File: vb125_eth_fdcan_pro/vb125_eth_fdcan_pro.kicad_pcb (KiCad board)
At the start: 2 copper layers, 2 parts, among them U1 STM32H725IGKx, U2 LAN8740A

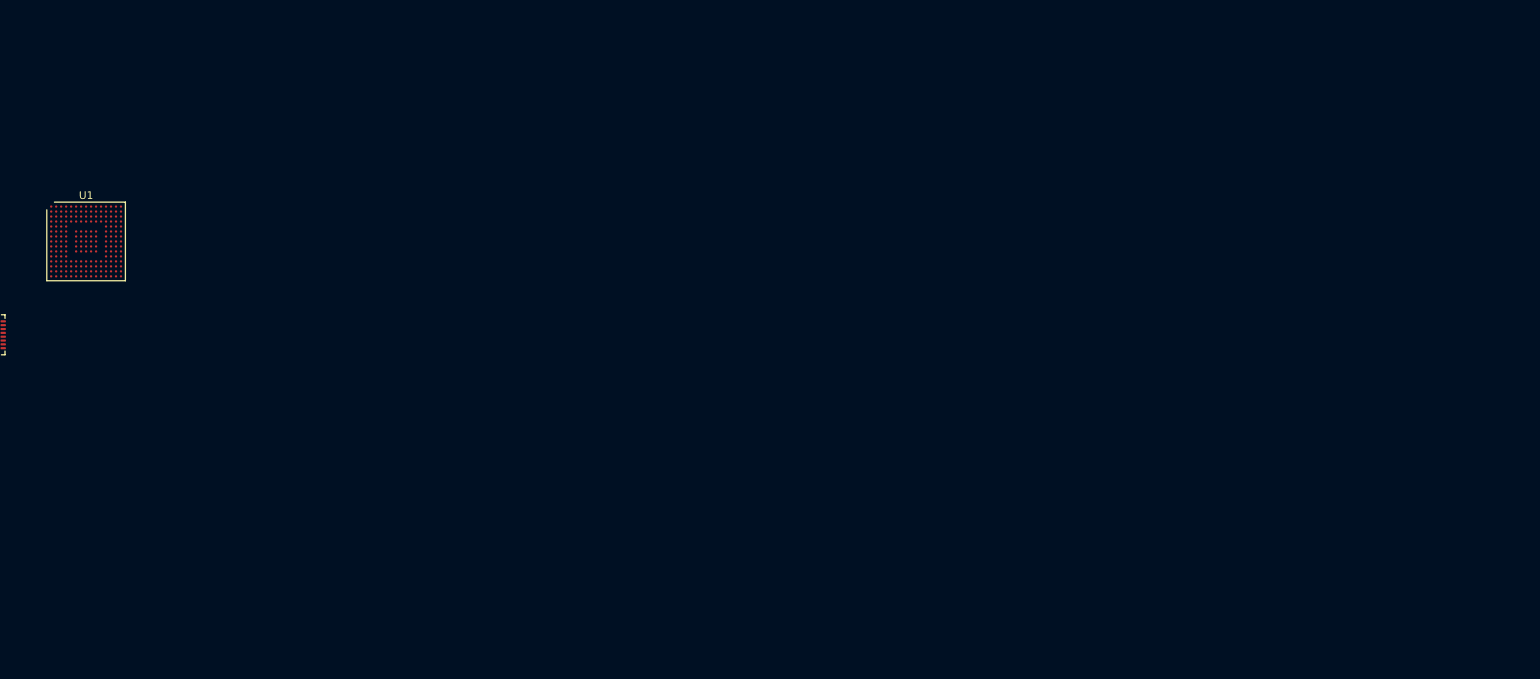
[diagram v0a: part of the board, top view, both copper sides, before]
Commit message: Work on PoE. Rearrange pages.
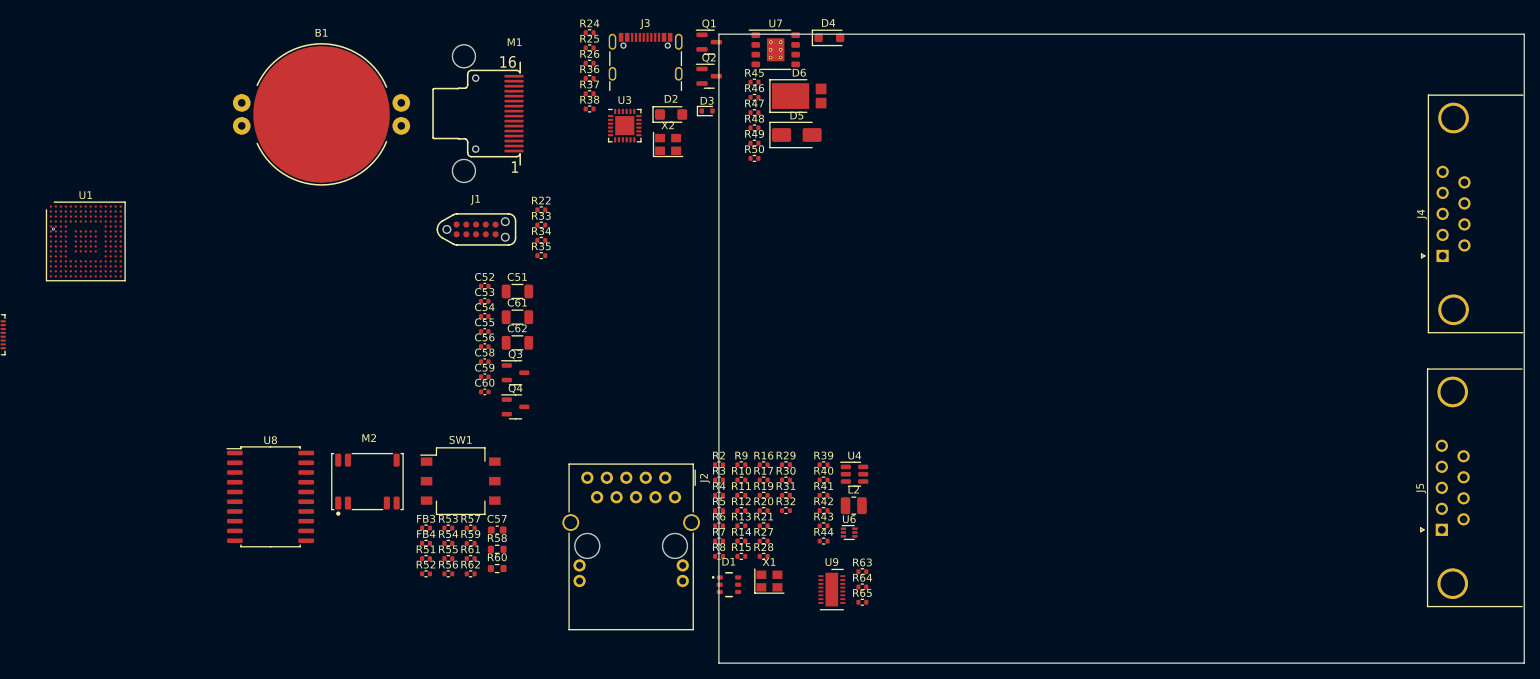
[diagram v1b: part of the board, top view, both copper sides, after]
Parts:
- added B1: BAT-HLD-001-THM, vhrd_connector_battery:BAT-HLD-001-THM, F.Cu at (97.4, 48.3)
- added C51: 10.0uF ±10% 10V X7R, Capacitor_SMD:C_1206_3216Metric, F.Cu at (122.9, 71.3)
- added C52: 50V_100nF_X7R, Capacitor_SMD:C_0402_1005Metric, F.Cu at (118.7, 70.7)
- added C53: X7R_10nF_50V, Capacitor_SMD:C_0402_1005Metric, F.Cu at (118.7, 72.6)
- added C54: 50V_100nF_X7R, Capacitor_SMD:C_0402_1005Metric, F.Cu at (118.7, 74.6)
- added C55: X7R_10nF_50V, Capacitor_SMD:C_0402_1005Metric, F.Cu at (118.7, 76.6)
- added C56: 5.0pF, Capacitor_SMD:C_0402_1005Metric, F.Cu at (118.7, 78.5)
- added C57: 4.7uF ±10% 6.3V, Capacitor_SMD:C_0603_1608Metric, F.Cu at (120.3, 102.5)
- added C58: 10.0nF ±10% 50V X7R, Capacitor_SMD:C_0402_1005Metric, F.Cu at (118.7, 80.5)
- added C59: 0.1uF 10% X7R 50V, Capacitor_SMD:C_0402_1005Metric, F.Cu at (118.7, 82.5)
- added C60: 220.0nF ±10% 10V X7R, Capacitor_SMD:C_0402_1005Metric, F.Cu at (118.7, 84.4)
- added C61: 10.0uF ±10% 10V X7R, Capacitor_SMD:C_1206_3216Metric, F.Cu at (122.9, 74.7)
- added C62: 10.0uF ±10% 10V X7R, Capacitor_SMD:C_1206_3216Metric, F.Cu at (122.9, 78.0)
- added D1: D5V0P4UR6SO-7, vhrd_passive_tvs:D5V0P4UR6SO-7, F.Cu at (150.5, 109.6)
- added D2: SMF22A, Diode_SMD:D_SMF, F.Cu at (143.0, 48.3)
- added D3: MM5Z10VT1G, Diode_SMD:D_SOD-523, F.Cu at (147.7, 47.8)
- added D4: RB168MM150TFTR, Diode_SMD:D_SOD-123F, F.Cu at (163.6, 38.3)
- added D5: CMZ5944B, Diode_SMD:D_SMA, F.Cu at (159.4, 50.9)
- added D6: PDS835L-13, Diode_SMD:D_PowerDI-5, F.Cu at (159.7, 45.9)
- added FB3: 100MHz_1.8KOhm, Resistor_SMD:R_0402_1005Metric, F.Cu at (111.0, 102.2)
- added FB4: BLM15BX182SN1D_100MHz_1.8KOhm, Resistor_SMD:R_0402_1005Metric, F.Cu at (111.0, 104.2)
- added J1: TAGconnect NL, vhrd_connector_debug:TC2050-IDC-NL, F.Cu at (117.5, 63.3)
- added J2: ARJM11C7-114-BA-EW2, vhrd_connector_abracon:RJ45_Abracon_ARJM11_7POE_LED, F.Cu at (132.0, 95.6)
- added J3: USB_C_Receptacle_USB2.0, Connector_USB:USB_C_Receptacle_GCT_USB4105-xx-A_16P_TopMnt_Horizontal, F.Cu at (139.6, 41.9)
- added J4: D09P33E4GL00LF, vhrd_connector_amphenol:D09P33E4GL00LF, F.Cu at (243.6, 66.7)
- added J5: D09P33E4GL00LF, vhrd_connector_amphenol:D09P33E4GL00LF, F.Cu at (243.4, 102.4)
- added L2: DFE252010F-1R0M=P2, Inductor_SMD:L_1008_2520Metric, F.Cu at (166.8, 99.3)
- added M1: DM-OLED042-647, vhrd_opto_display:DM-OLED042-647, F.Cu at (122.5, 48.2)
- added M2: B0505MT-1WR4, vhrd_module_power:B0505MT-1WR4, F.Cu at (103.4, 96.1)
- added Q1: BSS138, Package_TO_SOT_SMD:SOT-23, F.Cu at (147.9, 38.8)
- added Q2: BSS138, Package_TO_SOT_SMD:SOT-23, F.Cu at (147.9, 43.3)
- added Q3: FDN358P, Package_TO_SOT_SMD:SOT-23-3, F.Cu at (122.7, 81.9)
- added Q4: FDN358P, Package_TO_SOT_SMD:SOT-23-3, F.Cu at (122.7, 86.4)
- added R10: 10k, Resistor_SMD:R_0402_1005Metric, F.Cu at (152.1, 95.9)
- added R11: 33R, Resistor_SMD:R_0402_1005Metric, F.Cu at (152.1, 97.9)
- added R12: 33R, Resistor_SMD:R_0402_1005Metric, F.Cu at (152.1, 99.9)
- added R13: 33R, Resistor_SMD:R_0402_1005Metric, F.Cu at (152.1, 101.9)
- added R14: 10k, Resistor_SMD:R_0402_1005Metric, F.Cu at (152.1, 103.9)
- added R15: 10k, Resistor_SMD:R_0402_1005Metric, F.Cu at (152.1, 105.9)
- added R16: 10k, Resistor_SMD:R_0402_1005Metric, F.Cu at (155.0, 93.9)
- added R17: 12k1, Resistor_SMD:R_0402_1005Metric, F.Cu at (155.0, 95.9)
- added R19: ?R, Resistor_SMD:R_0402_1005Metric, F.Cu at (155.0, 97.9)
- added R2: 10k, Resistor_SMD:R_0402_1005Metric, F.Cu at (149.2, 93.9)
- added R20: ?R, Resistor_SMD:R_0402_1005Metric, F.Cu at (155.0, 99.9)
- added R21: ?R, Resistor_SMD:R_0402_1005Metric, F.Cu at (155.0, 101.9)
- added R22: 49R9, Resistor_SMD:R_0402_1005Metric, F.Cu at (126.0, 60.7)
- added R24: ?R, Resistor_SMD:R_0402_1005Metric, F.Cu at (132.3, 37.6)
- added R25: ?R, Resistor_SMD:R_0402_1005Metric, F.Cu at (132.3, 39.6)
- added R26: ?R, Resistor_SMD:R_0402_1005Metric, F.Cu at (132.3, 41.6)
- added R27: 49R9, Resistor_SMD:R_0402_1005Metric, F.Cu at (155.0, 103.9)
- added R28: 49R9, Resistor_SMD:R_0402_1005Metric, F.Cu at (155.0, 105.9)
- added R29: 49R9, Resistor_SMD:R_0402_1005Metric, F.Cu at (157.9, 93.9)
- added R3: 10k, Resistor_SMD:R_0402_1005Metric, F.Cu at (149.2, 95.9)
- added R30: 49R9, Resistor_SMD:R_0402_1005Metric, F.Cu at (157.9, 95.9)
- added R31: 1K, Resistor_SMD:R_0402_1005Metric, F.Cu at (157.9, 97.9)
- added R32: 1K, Resistor_SMD:R_0402_1005Metric, F.Cu at (157.9, 99.9)
- added R33: 0, Resistor_SMD:R_0402_1005Metric, F.Cu at (126.0, 62.7)
- added R34: 10K, Resistor_SMD:R_0402_1005Metric, F.Cu at (126.0, 64.7)
- added R35: 10K, Resistor_SMD:R_0402_1005Metric, F.Cu at (126.0, 66.7)
- added R36: 5K1, Resistor_SMD:R_0402_1005Metric, F.Cu at (132.3, 43.6)
- added R37: 5K1, Resistor_SMD:R_0402_1005Metric, F.Cu at (132.3, 45.6)
- added R38: 5K1, Resistor_SMD:R_0402_1005Metric, F.Cu at (132.3, 47.6)
- added R39: 301K, Resistor_SMD:R_0402_1005Metric, F.Cu at (162.8, 93.9)
- added R4: 10k, Resistor_SMD:R_0402_1005Metric, F.Cu at (149.2, 97.9)
- added R40: 0, Resistor_SMD:R_0402_1005Metric, F.Cu at (162.8, 95.9)
- added R41: 100K, Resistor_SMD:R_0402_1005Metric, F.Cu at (162.8, 97.9)
- added R42: 100K, Resistor_SMD:R_0402_1005Metric, F.Cu at (162.8, 99.9)
- added R43: 45k, Resistor_SMD:R_0402_1005Metric, F.Cu at (162.8, 101.9)
- added R44: 10k, Resistor_SMD:R_0402_1005Metric, F.Cu at (162.8, 103.9)
- added R45: 1M, Resistor_SMD:R_0402_1005Metric, F.Cu at (153.8, 44.1)
- added R46: 348K, Resistor_SMD:R_0402_1005Metric, F.Cu at (153.8, 46.0)
- added R47: 10K, Resistor_SMD:R_0402_1005Metric, F.Cu at (153.8, 48.0)
- added R48: ?R, Resistor_SMD:R_0402_1005Metric, F.Cu at (153.8, 50.0)
- added R49: 158K, Resistor_SMD:R_0402_1005Metric, F.Cu at (153.8, 52.0)
- added R5: 10k, Resistor_SMD:R_0402_1005Metric, F.Cu at (149.2, 99.9)
- added R50: 100R, Resistor_SMD:R_0402_1005Metric, F.Cu at (153.8, 54.0)
- added R51: 0, Resistor_SMD:R_0402_1005Metric, F.Cu at (111.0, 106.2)
- added R52: 47K 1%, Resistor_SMD:R_0402_1005Metric, F.Cu at (111.0, 108.2)
- added R53: 0, Resistor_SMD:R_0402_1005Metric, F.Cu at (113.9, 102.2)
- added R54: 47K 1%, Resistor_SMD:R_0402_1005Metric, F.Cu at (113.9, 104.2)
- added R55: 0, Resistor_SMD:R_0402_1005Metric, F.Cu at (113.9, 106.2)
- added R56: 100K 1%, Resistor_SMD:R_0402_1005Metric, F.Cu at (113.9, 108.2)
- added R57: 0, Resistor_SMD:R_0402_1005Metric, F.Cu at (116.8, 102.2)
- added R58: 56R, Resistor_SMD:R_0603_1608Metric, F.Cu at (120.3, 105.0)
- added R59: 100K 1%, Resistor_SMD:R_0402_1005Metric, F.Cu at (116.8, 104.2)
- added R6: 10k, Resistor_SMD:R_0402_1005Metric, F.Cu at (149.2, 101.9)
- added R60: 56R, Resistor_SMD:R_0603_1608Metric, F.Cu at (120.3, 107.5)
- added R61: 0, Resistor_SMD:R_0402_1005Metric, F.Cu at (116.8, 106.2)
- added R62: 0, Resistor_SMD:R_0402_1005Metric, F.Cu at (116.8, 108.2)
- added R63: DNP, Resistor_SMD:R_0402_1005Metric, F.Cu at (167.9, 107.9)
- added R64: DNP, Resistor_SMD:R_0402_1005Metric, F.Cu at (167.9, 109.9)
- added R65: DNP, Resistor_SMD:R_0402_1005Metric, F.Cu at (167.9, 111.9)
- added R7: 1k5, Resistor_SMD:R_0402_1005Metric, F.Cu at (149.2, 103.9)
- added R8: 10k, Resistor_SMD:R_0402_1005Metric, F.Cu at (149.2, 105.9)
- added R9: 10k, Resistor_SMD:R_0402_1005Metric, F.Cu at (152.1, 93.9)
- added SW1: DS04-254-2-03BK-SMT, Button_Switch_SMD:SW_DIP_SPSTx03_Slide_Omron_A6S-310x_W8.9mm_P2.54mm, F.Cu at (115.5, 96.1)
- added U3: USB3315, vhrd_interface_usb:QFN24_MICROCHIP, F.Cu at (136.9, 49.7)
- added U4: AOZ1282CI, Package_TO_SOT_SMD:SOT-23-6, F.Cu at (166.9, 95.2)
- added U6: RT5760A/B, Package_TO_SOT_SMD:SOT-563, F.Cu at (166.2, 102.8)
- added U7: LT8304IS8E#PBF, vhrd_generic:SOIC-8-ANALOG, F.Cu at (156.6, 39.8)
- added U8: ADM3057E, Package_SO:SOIC-20W_7.5x12.8mm_P1.27mm, F.Cu at (90.7, 98.1)
- added U9: LTC4267, Package_DFN_QFN:DFN-16-1EP_3x5mm_P0.5mm_EP1.66x4.4mm, F.Cu at (163.9, 110.2)
- added X1: 50MHz, Oscillator:Oscillator_SMD_Abracon_ASE-4Pin_3.2x2.5mm, F.Cu at (155.8, 109.1)
- added X2: 24MHz, Oscillator:Oscillator_SMD_Abracon_ASE-4Pin_3.2x2.5mm, F.Cu at (142.6, 52.2)
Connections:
- U1 pad A10: unconnected-(U1D-PD1-PadA10) -> FDCAN1_TX
- U1 pad A12: unconnected-(U1A-PA14-PadA12) -> /MCU_H7/H7_SWCLK
- U1 pad A13: unconnected-(U1I-VDDLDO-PadA13) -> /MCU_H7/VDDLDO
- U1 pad A14: unconnected-(U1I-VCAP-PadA14) -> /MCU_H7/VCAP
- U1 pad A2: unconnected-(U1B-PB8-PadA2) -> FDCAN1_RX
- U1 pad A3: unconnected-(U1I-VDDLDO-PadA3) -> /MCU_H7/VDDLDO
- U1 pad A4: unconnected-(U1I-VCAP-PadA4) -> /MCU_H7/VCAP
- U1 pad A7: unconnected-(U1G-PG11-PadA7) -> ETH_TXEN
- U1 pad A8: unconnected-(U1G-PG9-PadA8) -> FDCAN3_TX
- U1 pad B10: unconnected-(U1D-PD2-PadB10) -> SDMMC_CMD
- U1 pad B11: unconnected-(U1C-PC12-PadB11) -> SDMMC_CK
- U1 pad B13: unconnected-(U1A-PA13-PadB13) -> /MCU_H7/H7_SWDIO
- U1 pad B7: unconnected-(U1G-PG13-PadB7) -> ETH_TXD0
- U1 pad C11: unconnected-(U1C-PC11-PadC11) -> SDMMC_D3
- U1 pad C12: unconnected-(U1C-PC10-PadC12) -> SDMMC_D2
- U1 pad C5: unconnected-(U1I-BOOT0-PadC5) -> /MCU_H7/BOOT0
- U1 pad C6: unconnected-(U1B-PB5-PadC6) -> ULPI_D7
- U1 pad C7: unconnected-(U1G-PG14-PadC7) -> ETH_TXD1
- U1 pad C8: unconnected-(U1G-PG10-PadC8) -> FDCAN3_RX
- U1 pad D11: unconnected-(U1I-VDD-PadD11) -> +3V3_DCDC
- U1 pad D14: unconnected-(U1C-PC8-PadD14) -> SDMMC_D0
- U1 pad D4: unconnected-(U1I-PDR_ON-PadD4) -> Net-(U1I-PDR_ON)
- U1 pad D5: unconnected-(U1I-VDD-PadD5) -> +3V3_DCDC
- U1 pad E12: unconnected-(U1I-VDD-PadE12) -> +3V3_DCDC
- U1 pad E13: unconnected-(U1C-PC9-PadE13) -> SDMMC_D1
- U1 pad E15: unconnected-(U1I-VDD50USB-PadE15) -> +3V3_DCDC
- U1 pad E2: unconnected-(U1I-VBAT-PadE2) -> /MCU_H7/VBAT
- U1 pad E4: unconnected-(U1I-VDD-PadE4) -> +3V3_DCDC
- U1 pad F1: unconnected-(U1I-VLXSMPS-PadF1) -> /MCU_H7/VLX
- U1 pad F13: unconnected-(U1I-VDD33USB-PadF13) -> +3V3_DCDC
- U1 pad F2: unconnected-(U1I-VSSSMPS-PadF2) -> GND
- U1 pad G1: unconnected-(U1I-VDDSMPS-PadG1) -> /MCU_H7/VDDSMPS
- U1 pad G2: unconnected-(U1I-VFBSMPS-PadG2) -> /MCU_H7/VDDLDO
- U1 pad G4: unconnected-(U1I-VDD-PadG4) -> +3V3_DCDC
- U1 pad H12: unconnected-(U1I-VDD-PadH12) -> +3V3_DCDC
- U1 pad J1: unconnected-(U1H-PH0-OSC_IN-PadJ1) -> H7_CLK
- U1 pad K4: unconnected-(U1I-VDD-PadK4) -> +3V3_DCDC
- U1 pad L1: unconnected-(U1I-NRST-PadL1) -> /MCU_H7/~{H7_RST}
- U1 pad L12: unconnected-(U1I-VDD-PadL12) -> +3V3_DCDC
- U1 pad L15: unconnected-(U1B-PB13-PadL15) -> ULPI_D6
- U1 pad L2: unconnected-(U1C-PC0-PadL2) -> ULPI_STP
- U1 pad L3: unconnected-(U1C-PC1-PadL3) -> ETH_MDC
- U1 pad L4: unconnected-(U1I-VREF--PadL4) -> GND
- U1 pad M1: unconnected-(U1C-PC2-PadM1) -> ULPI_DIR
- U1 pad M15: unconnected-(U1B-PB12-PadM15) -> ULPI_D5
- U1 pad M2: unconnected-(U1C-PC3-PadM2) -> ULPI_NXT
- U1 pad M3: unconnected-(U1I-VREF+-PadM3) -> /MCU_H7/VDDA
- U1 pad M4: unconnected-(U1I-VDDA-PadM4) -> /MCU_H7/VDDA
- U1 pad M5: unconnected-(U1I-VDD-PadM5) -> +3V3_DCDC
- U1 pad M7: unconnected-(U1C-PC5-PadM7) -> ETH_RXD1
- U1 pad M8: unconnected-(U1B-PB1-PadM8) -> ULPI_D2
- U1 pad M9: unconnected-(U1I-VDD-PadM9) -> +3V3_DCDC
- U1 pad N12: unconnected-(U1B-PB10-PadN12) -> ULPI_D3
- U1 pad N3: unconnected-(U1I-VSSA-PadN3) -> GND
- U1 pad N4: /MCU_H7/TXD0 -> unconnected-(U1H-PH2-PadN4)
- U1 pad N5: unconnected-(U1A-PA3-PadN5) -> ULPI_D0
- U1 pad N6: unconnected-(U1A-PA7-PadN6) -> ETH_CRS_DV
- U1 pad P10: unconnected-(U1B-PB11-PadP10) -> ULPI_D4
- U1 pad P2: unconnected-(U1A-PA1-PadP2) -> ETH_REFCLK
- U1 pad P4: /MCU_H7/TXD2 -> unconnected-(U1H-PH4-PadP4)
- U1 pad P6: unconnected-(U1A-PA5-PadP6) -> ULPI_CK
- U1 pad R13: unconnected-(U1I-VCAP-PadR13) -> /MCU_H7/VCAP
- U1 pad R14: unconnected-(U1I-VDDLDO-PadR14) -> /MCU_H7/VDDLDO
- U1 pad R2: unconnected-(U1A-PA2-PadR2) -> ETH_MDIO
- U1 pad R4: /MCU_H7/TXD1 -> unconnected-(U1H-PH3-PadR4)
- U1 pad R5: /MCU_H7/TXD3 -> unconnected-(U1H-PH5-PadR5)
- U1 pad R6: unconnected-(U1C-PC4-PadR6) -> ETH_RXD0
- U1 pad R8: unconnected-(U1B-PB0-PadR8) -> ULPI_D1
- U2 pad 1: unconnected-(U2B-VDD2A-Pad1) -> /Eth/+AVDD_PHY
- U2 pad 10: unconnected-(U2A-RXD1/MODE1-Pad10) -> /Eth/RXD1
- U2 pad 11: unconnected-(U2A-RXD0/MODE0-Pad11) -> /Eth/RXD0
- U2 pad 12: unconnected-(U2B-VDDIO-Pad12) -> +3V3_DCDC
- U2 pad 13: unconnected-(U2A-RXER/RXD4/PHYAD0-Pad13) -> /Eth/PHYAD0
- U2 pad 15: unconnected-(U2A-COL/CRS_DV/MODE2-Pad15) -> Net-(U2A-COL/CRS_DV/MODE2)
- U2 pad 16: unconnected-(U2A-MDIO-Pad16) -> ETH_MDIO
- U2 pad 17: unconnected-(U2A-MDC-Pad17) -> ETH_MDC
- U2 pad 18: unconnected-(U2A-~{INT}/TXER/TXD4-Pad18) -> Net-(U2A-~{INT}/TXER/TXD4)
- U2 pad 19: unconnected-(U2A-~{RST}-Pad19) -> ~{ETH_PHY_RST}
- U2 pad 2: unconnected-(U2A-LED2/~{INT}/~{PME}/~{INTSEL}-Pad2) -> ~{ETH_INT_PME}
- U2 pad 21: unconnected-(U2A-TXEN-Pad21) -> ETH_TXEN
- U2 pad 22: /Eth/TXD0 -> ETH_TXD0
- U2 pad 23: /Eth/TXD1 -> ETH_TXD1
- U2 pad 24: /Eth/TXD2 -> /Eth/TXD2_NU
- U2 pad 25: /Eth/TXD3 -> /Eth/TXD3_NU
- U2 pad 27: unconnected-(U2B-VDD1A-Pad27) -> /Eth/+AVDD_PHY
- U2 pad 28: unconnected-(U2A-TXN-Pad28) -> Net-(D1-I/O_2)
- U2 pad 29: unconnected-(U2A-TXP-Pad29) -> Net-(D1-I/O_3)
- U2 pad 30: unconnected-(U2A-RXN-Pad30) -> Net-(D1-I/O_1)
- U2 pad 31: unconnected-(U2A-RXP-Pad31) -> Net-(D1-I/O_4)
- U2 pad 32: unconnected-(U2B-RBIAS-Pad32) -> /Eth/RBIAS
- U2 pad 5: unconnected-(U2A-XTAL1/CLKIN-Pad5) -> Net-(U2A-XTAL1/CLKIN)
- U2 pad 6: unconnected-(U2B-VDDCR-Pad6) -> /Eth/VDDCR_PHY
- U2 pad 7: unconnected-(U2A-RXCLK/PHYAD1-Pad7) -> /Eth/PHYAD1
- U2 pad 8: unconnected-(U2A-RXD3/PHYAD2-Pad8) -> /Eth/PHYAD2
- U2 pad 9: unconnected-(U2A-RXD2/~{PME}/RMIISEL-Pad9) -> /Eth/RXD2_NU
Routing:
- net /MCU_H7/VLX: vias 0 -> 1
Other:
- board outline added: 105 x 82 mm
- copper layers 2 -> 4
- rule pad_to_mask_clearance: 0 -> 0.05
